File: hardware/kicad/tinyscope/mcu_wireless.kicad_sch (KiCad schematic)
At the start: 0 parts

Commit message: feat: hardware: Add tinyscope kicad project. Adds Raytac MDBT50Q #1
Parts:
- added U11: MDBT50Q-1MV2, RF_Module:Raytac_MDBT50Q, symbol RF_Module:MDBT50Q-1MV2
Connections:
- new net: U11.1 (GND), U11.15 (GND), U11.2 (GND), U11.33 (GND), U11.55 (GND)
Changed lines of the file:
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@@
 (kicad_sch (version 20230121) (generator eeschema)
   (paper "A4")
+  (symbol (lib_id "RF_Module:MDBT50Q-1MV2") (at 139.7 86.36 0) (unit 1)
+    (in_bom yes) (on_board yes) (dnp no)
+    (property "Reference" "U11" (at 153.67 41.91 0)
+      (effects (font (size 1.27 1.27)) (justify left))
+    )
+    (property "Value" "MDBT50Q-1MV2" (at 142.24 131.445 0)
+      (effects (font (size 1.27 1.27)) (justify left))
+    )
+    (property "Footprint" "RF_Module:Raytac_MDBT50Q" (at 139.7 91.44 0)
+      (effects (font (size 1.27 1.27)) hide)
+    )
+    (property "Datasheet" "https://www.raytac.com/download/index.php?index_id=43" (at 139.7 91.44 0)
+      (effects (font (size 1.27 1.27)) hide)
+    )
+    (pin "1")
+    (pin "10")
+    (pin "11")
+    (pin "12")
+    (pin "13")
+    (pin "14")
+    (pin "15")
+    (pin "16")
+    (pin "17")
+    (pin "18")
+    (pin "19")
+    (pin "2")
+    (pin "20")
+    (pin "21")
+    (pin "22")
+    (pin "23")
+    (pin "24")
+    (pin "25")
+    (pin "26")
+    (pin "27")
+    (pin "28")
+    (pin "29")
+    (pin "3")
+    (pin "30")
+    (pin "31")
+    (pin "32")
+    (pin "33")
+    (pin "34")
+    (pin "35")
+    (pin "36")
+    (pin "37")
+    (pin "38")
+    (pin "39")
+    (pin "4")
+    (pin "40")
+    (pin "41")
+    (pin "42")
+    (pin "43")
+    (pin "44")
+    (pin "45")
+    (pin "46")
+    (pin "47")
+    (pin "48")
+    (pin "49")
+    (pin "5")
+    (pin "50")
+    (pin "51")
+    (pin "52")
+    (pin "53")
+    (pin "54")
+    (pin "55")
+    (pin "56")
+    (pin "57")
+    (pin "58")
+    (pin "59")
+    (pin "6")
+    (pin "60")
+    (pin "61")
+    (pin "7")
+    (pin "8")
+    (pin "9")
+    (instances
+      (project "tinyscope"
+        (path "/bb072e32-cc57-415a-8554-0e84d374f333/8ab32ff2-1997-48a8-8f3b-8df038411955"
+          (reference "U11") (unit 1)
+        )
+      )
+    )
+  )
 )

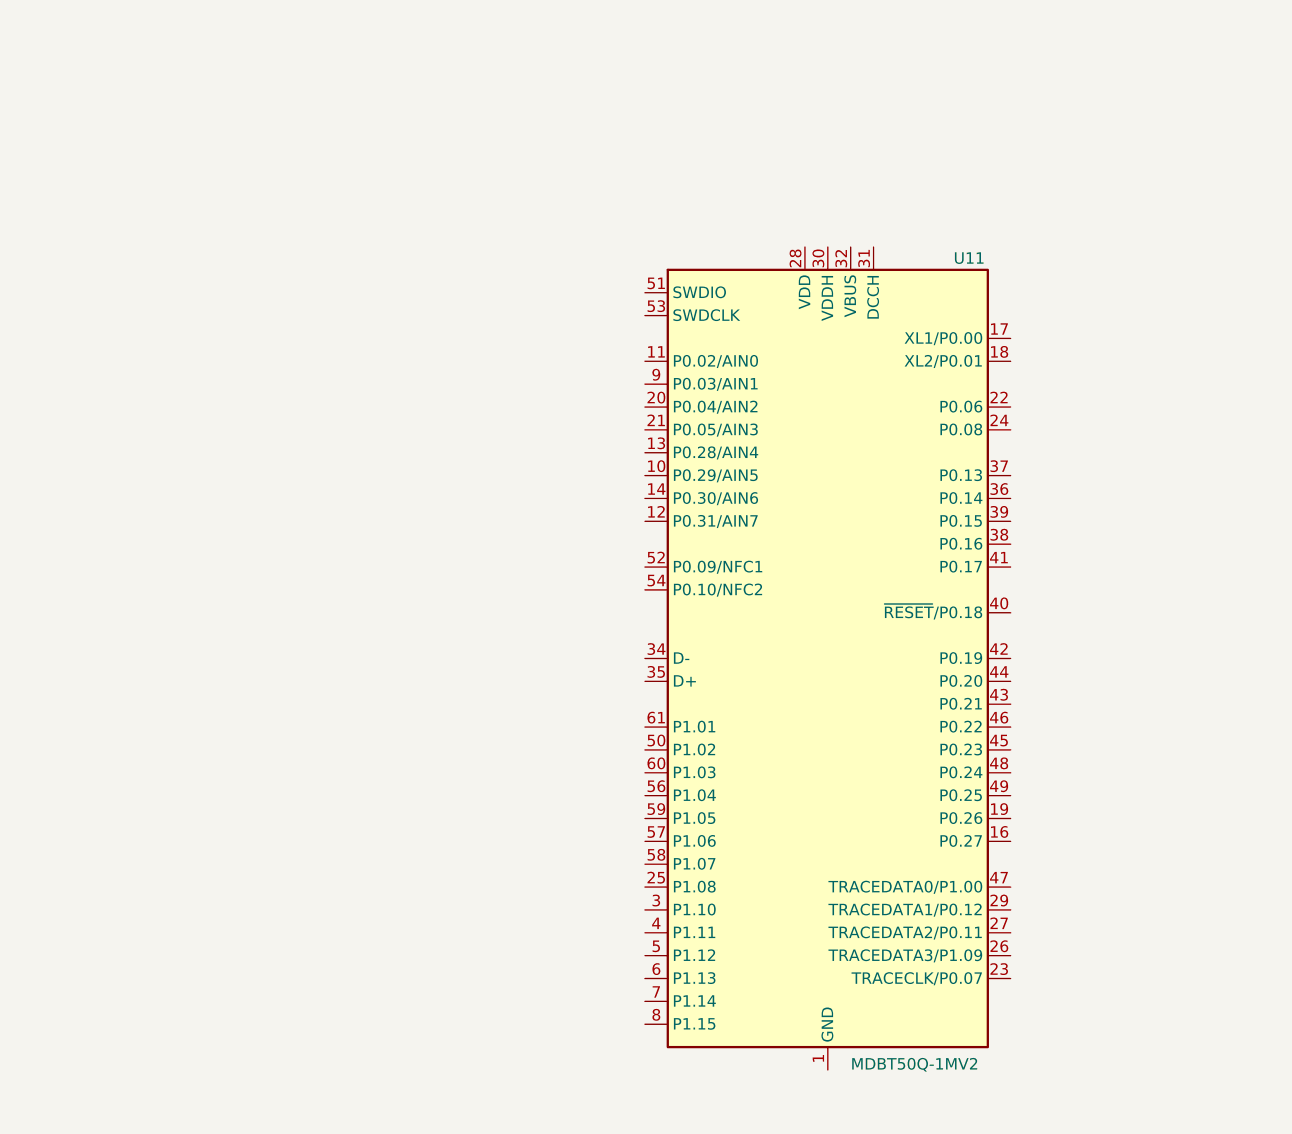
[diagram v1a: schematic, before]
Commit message: feat: hardware: Add tinyscope kicad project. Adds Raytac MDBT50Q #2. Basic schemtic with TAG Connect
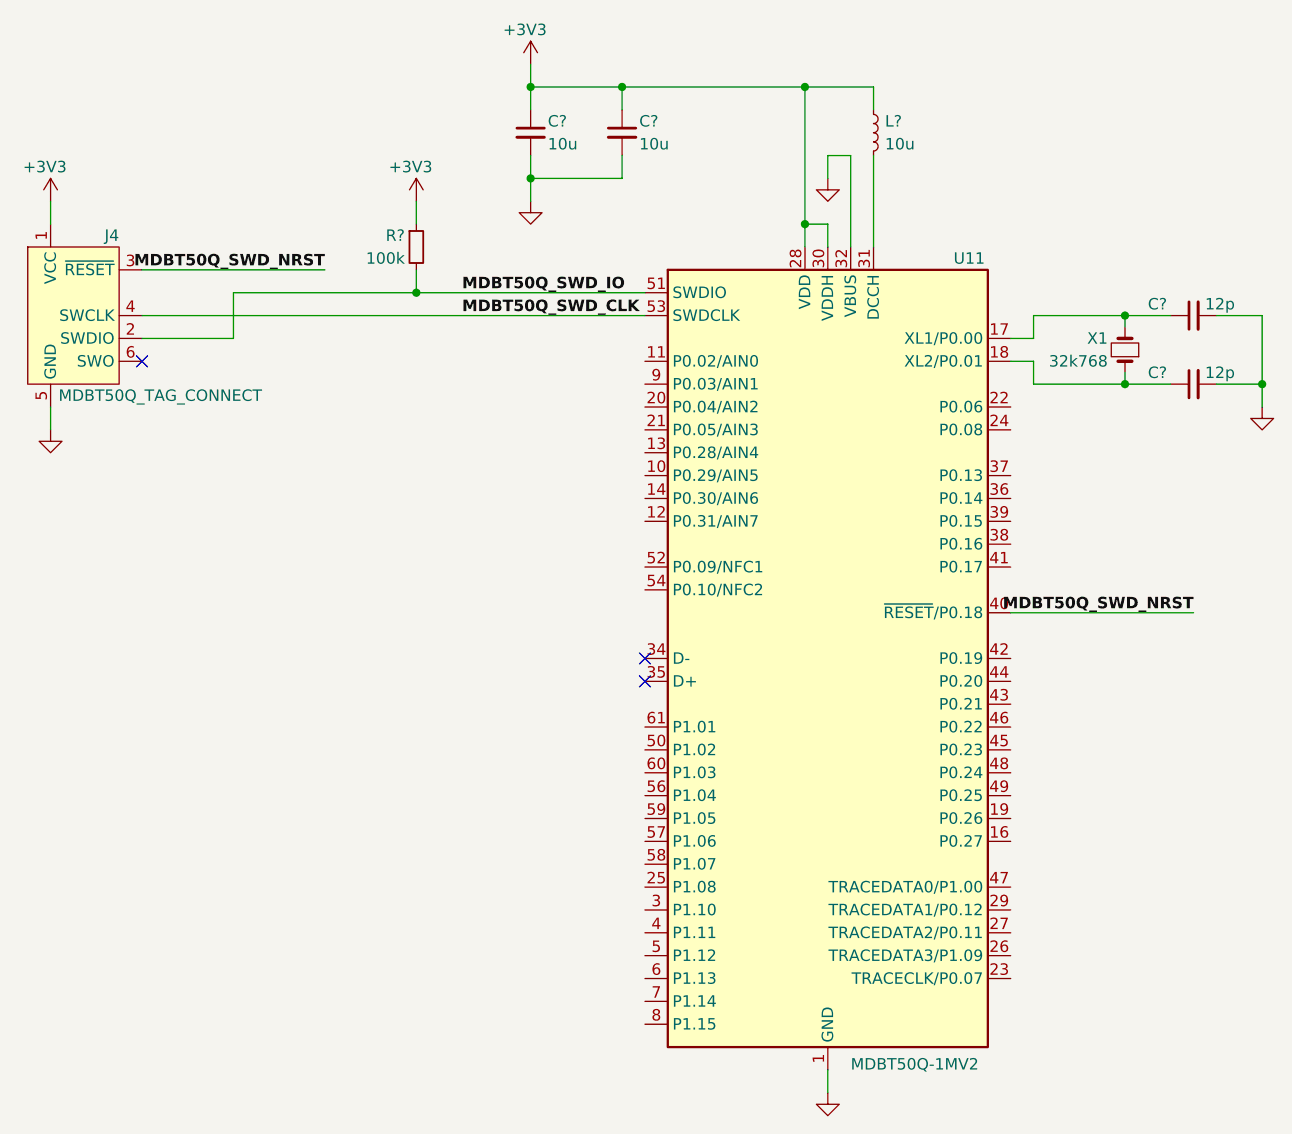
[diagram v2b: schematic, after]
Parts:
- added C? (x2): 12p, symbol Device:C_Small
- added C? (x2): 10u, symbol Device:C_Small
- added J4: MDBT50Q_TAG_CONNECT, Connector:Tag-Connect_TC2030-IDC-NL_2x03_P1.27mm_Vertical, symbol Connector:Conn_ARM_SWD_TagConnect_TC2030-NL
- added L?: 10u, symbol Device:L_Small
- added R?: 100k, symbol Device:R_Small
- added X1: 32k768, symbol Device:Crystal_Small
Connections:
- net GND: now reaches U11.1 (GND), U11.15 (GND), U11.2 (GND), U11.33 (GND), U11.55 (GND)
- net GND: now also U11.32 (VBUS), C?.2, C?.2, C?.2, C?.2, J4.5 (GND)
- net at U11.17 (XL1/P0.00): now also C?.1, X1.2
- net at U11.18 (XL2/P0.01): now also C?.1, X1.1
- net +3V3: now reaches U11.28 (VDD)
- net +3V3: now also U11.30 (VDDH), C?.1, C?.1, J4.1 (VCC), L?.1, R?.1
- net at U11.31 (DCCH): now also L?.2
- net MDBT50Q_SWD_NRST: now reaches U11.40 (~{RESET}/P0.18)
- net MDBT50Q_SWD_NRST: now also J4.3 (~{RESET})
- net MDBT50Q_SWD_IO: now reaches U11.51 (SWDIO)
- net MDBT50Q_SWD_IO: now also J4.2 (SWDIO), R?.2
- net MDBT50Q_SWD_CLK: now reaches U11.53 (SWDCLK)
- net MDBT50Q_SWD_CLK: now also J4.4 (SWCLK)
- no-connect marks 0 -> 3

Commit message: feat: doc: Update schematics - title and revision
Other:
- title: (none) -> Wireless MCU
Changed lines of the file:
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@@
 (kicad_sch (version 20230121) (generator eeschema)
   (paper "A4")
+  (title_block
+    (title "Wireless MCU")
+    (rev "v0.1")
+  )
   (junction (at 187.96 55.88) (diameter 0) (color 0 0 0 0)
   )
